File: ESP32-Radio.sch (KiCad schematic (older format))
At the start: 67 parts, among them J1 Jack-DC, J11 Conn_01x04_Female, J2 BNC, J6 Audio_Jack, Q1 2N3904-SMD, Q2 2SC5706, Q3 2SC5706, T1 T37_XFRM, U1 LM358, U10 si5351, U11 LD33V, U2 LM358, U6 MCP1703A-2502_SOT223, U8 FST3253

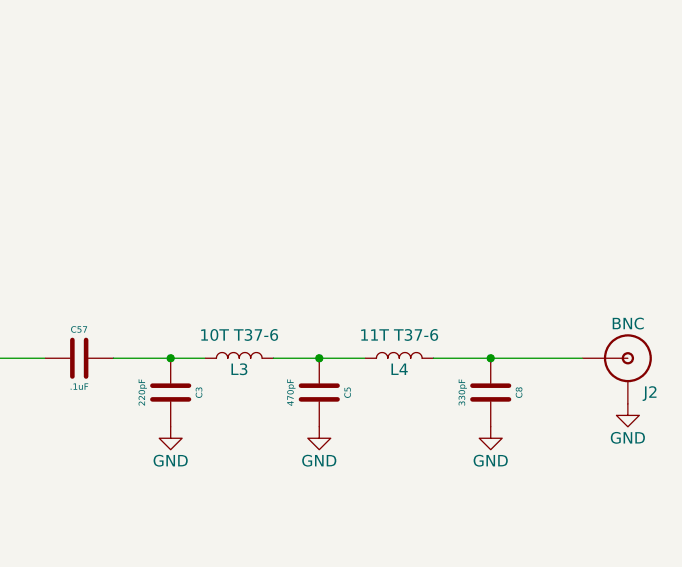
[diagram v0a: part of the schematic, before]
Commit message: added trap to lowpass
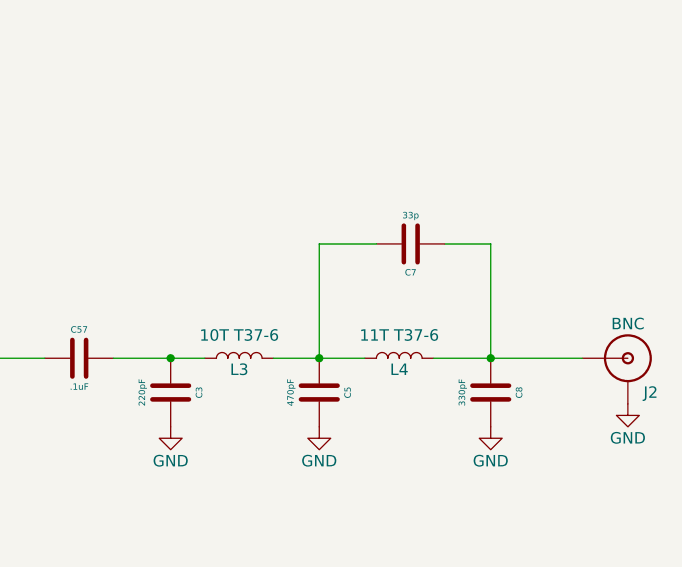
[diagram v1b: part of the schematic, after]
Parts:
- added C7: 33p, Xenir:Capacitor 1206, symbol Xenir:Capacitor
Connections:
- net at C8.1, J2.S (OUT), L4.2: now also C7.1
- net at C5.1, L3.2, L4.1: now also C7.2
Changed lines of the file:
@@
 	1    0    0    -1
 $EndComp
+$Comp
+L Xenir:Capacitor C7
+U 1 1 60F14082
+P 16550 7050
+F 0 "C7" H 16550 7175 28  0000 C CNN
+F 1 "33p" H 16550 6925 28  0000 C CNN
+F 2 "Xenir:Capacitor 1206" H 16550 6900 50  0001 C CNN
+F 3 "" H 16550 6900 50  0001 C CNN
+	1    16550 7050
+	-1   0    0    1
+$EndComp
+Wire Wire Line
+	16700 7050 16900 7050
+Wire Wire Line
+	16900 7050 16900 7550
+Wire Wire Line
+	16150 7050 16400 7050
+Wire Wire Line
+	16150 7050 16150 7550
 $EndSCHEMATC

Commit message: fixed rescue reference
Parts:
- removed R5: 1k, Xenir:Resistor 0805, symbol Xenir:Resistor
- removed T1: T37_XFRM, Xenir:T37 Transformer, symbol Xenir:T37_XFRM
- added C9: .1uF, Xenir:Capacitor 0805, symbol Xenir:Capacitor
- added R64, R65: 4.7k, Xenir:Resistor 0805, symbol Xenir:Resistor
- added R7, R8: 49.9, Xenir:Resistor 0805, symbol Xenir:Resistor
- added T1: T50_SPLITTER, Xenir:T50 Trifilar, symbol Xenir:T50_SPLITTER
- R4: symbol ESP32-Radio-rescue:0.3OHM-0805-1_8W-1%-phase_v3-eagle-import-IQ-Tayloe-Mixer-rescue -> Xenir:Resistor
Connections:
- net +2V5: now also T1.C2A, T1.C3B
- net +5V: now also R64.1
- net GND: now also R65.2, T1.C1B
- net at Q1.1 (B): now also C9.2, R64.2, R65.1
- net at U8.9 (2A): now also R7.2
- net at U8.7 (1A): now also R8.2
- new net: C9.1, T1.C1A
- new net: R8.1, T1.C2B
- new net: R7.1, T1.C3A
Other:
- moved on the sheet: J6
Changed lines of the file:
@@
 GND
 Wire Wire Line
-	9050 10700 9550 10700
-Wire Wire Line
 	10950 11600 11050 11600
 Wire Wire Line
@@
 Wire Wire Line
 	9150 12300 9150 11400
-$Comp
-L ESP32-Radio-rescue:GND-Tayloe_Detector_v5-eagle-import-IQ-Tayloe-Mixer-rescue #GND01
-U 1 1 12C122FD
-P 9550 11200
-F 0 "#GND01" H 9550 11200 50  0001 C CNN
-F 1 "GND" H 9550 11190 59  0000 C TNN
-F 2 "" H 9550 11200 50  0001 C CNN
-F 3 "" H 9550 11200 50  0001 C CNN
-	1    9550 11200
-	1    0    0    -1
-$EndComp
 $Comp
 L Xenir:Capacitor C30
@@
 $EndComp
 $Comp
-L ESP32-Radio-rescue:0.3OHM-0805-1_8W-1%-phase_v3-eagle-import-IQ-Tayloe-Mixer-rescue R4
+L Xenir:Resistor R4
 U 1 1 5EF82FCB
 P 3350 11900
@@
 	1    0    0    -1
 $EndComp
-Connection ~ 9550 11100
 Wire Wire Line
 	9550 10900 9550 11100
@@
 	0    1    1    0
 $EndComp
-Wire Wire Line
-	9300 9050 9300 10500
 Wire Wire Line
 	9300 10500 9550 10500
@@
 L Xenir:Audio_Jack J6
 U 1 1 5EBAA7D4
-P 1500 10350
-F 0 "J6" H 1100 10000 50  0000 C CNN
-F 1 "Audio_Jack" H 1500 10350 50  0000 C CNN
-F 2 "Xenir:Audio_Jack" H 1500 10350 50  0001 C CNN
-F 3 "" H 1500 10350 50  0001 C CNN
-	1    1500 10350
-	1    0    0    -1
-$EndComp
-Wire Wire Line
-	1700 10700 1700 10600
-Wire Wire Line
-	1700 10800 1700 10900
+P 1650 10400
+F 0 "J6" H 1250 10050 50  0000 C CNN
+F 1 "Audio_Jack" H 1650 10400 50  0000 C CNN
+F 2 "Xenir:Audio_Jack" H 1650 10400 50  0001 C CNN
+F 3 "" H 1650 10400 50  0001 C CNN
+	1    1650 10400
+	1    0    0    -1
+$EndComp
+Wire Wire Line
+	1850 10750 1850 10650
+Wire Wire Line
+	1850 10850 1850 10950
 $Comp
 L power:GND #PWR033
 U 1 1 5EC9FFD3
-P 2350 10550
-F 0 "#PWR033" H 2350 10300 50  0001 C CNN
-F 1 "GND" H 2350 10400 50  0000 C CNN
-F 2 "" H 2350 10550 50  0001 C CNN
-F 3 "" H 2350 10550 50  0001 C CNN
-	1    2350 10550
-	1    0    0    -1
-$EndComp
-Wire Wire Line
-	1700 10500 2350 10500
-Wire Wire Line
-	2350 10500 2350 10550
+P 2500 10600
+F 0 "#PWR033" H 2500 10350 50  0001 C CNN
+F 1 "GND" H 2500 10450 50  0000 C CNN
+F 2 "" H 2500 10600 50  0001 C CNN
+F 3 "" H 2500 10600 50  0001 C CNN
+	1    2500 10600
+	1    0    0    -1
+$EndComp
+Wire Wire Line
+	1850 10550 2500 10550
+Wire Wire Line
+	2500 10550 2500 10600
 $Comp
 L Xenir:Cap_Polarized C16
@@
 P 9300 6550
 F 0 "J11" H 9300 6750 50  0000 C CNN
-F 1 "Conn_01x04_Female" H 9300 6250 50  0000 C CNN
+F 1 "Conn_01x04_Female" V 9450 6550 50  0000 C CNN
 F 2 "Connector_PinHeader_2.54mm:PinHeader_1x04_P2.54mm_Vertical" H 9300 6550 50  0001 C CNN
 F 3 "~" H 9300 6550 50  0001 C CNN
@@
 $EndComp
 $Comp
-L Xenir:T37_XFRM T1
-U 1 1 60E9134B
-P 10150 8200
-F 0 "T1" H 10150 7350 50  0000 C CNN
-F 1 "T37_XFRM" H 10150 8200 50  0000 C CNN
-F 2 "Xenir:T37 Transformer" H 10150 8200 50  0001 C CNN
-F 3 "" H 10150 8200 50  0001 C CNN
-	1    10150 8200
-	1    0    0    -1
-$EndComp
-Wire Wire Line
-	9750 8950 9750 9150
-Wire Wire Line
-	9750 9150 10750 9150
-Wire Wire Line
-	10750 9150 10750 8350
-Wire Wire Line
-	10750 8350 10550 8350
-$Comp
-L Xenir:Resistor R5
-U 1 1 60EAA63C
-P 9300 8650
-F 0 "R5" H 9300 8725 28  0000 C CNN
-F 1 "1k" H 9300 8575 28  0000 C CNN
-F 2 "Xenir:Resistor 0805" H 9300 8550 50  0001 C CNN
-F 3 "" H 9300 8550 50  0001 C CNN
-	1    9300 8650
-	0    1    1    0
-$EndComp
-Wire Wire Line
-	9750 8350 9300 8350
-Wire Wire Line
-	9300 8350 9300 8450
-Wire Wire Line
-	10550 8950 10550 9050
-Wire Wire Line
-	10550 9050 9300 9050
-Wire Wire Line
-	9300 9050 9300 8850
-Connection ~ 9300 9050
-Wire Wire Line
-	9300 8350 9050 8350
-Wire Wire Line
-	9050 8350 9050 10700
-Connection ~ 9300 8350
-$Comp
 L Xenir:2N3904-SMD Q1
 U 1 1 60F3E262
@@
 	1    0    0    -1
 $EndComp
-Connection ~ 10750 8350
 $Comp
 L Xenir:Resistor R6
@@
 Wire Wire Line
 	6650 12000 7500 12000
-Text GLabel 1700 10800 2    50   Input ~ 0
+Text GLabel 1850 10850 2    50   Input ~ 0
 Q_Out
-Text GLabel 1700 10600 2    50   Input ~ 0
+Text GLabel 1850 10650 2    50   Input ~ 0
 I_Out
 Wire Wire Line
@@
 Wire Wire Line
 	16150 7050 16150 7550
+$Comp
+L Xenir:T50_SPLITTER T1
+U 1 1 60EFEA4B
+P 9850 9350
+F 0 "T1" H 9850 8100 50  0000 C CNN
+F 1 "T50_SPLITTER" H 9850 9250 50  0000 C CNN
+F 2 "Xenir:T50 Trifilar" H 9850 9350 50  0001 C CNN
+F 3 "" H 9850 9350 50  0001 C CNN
+	1    9850 9350
+	-1   0    0    1
+$EndComp
+Wire Wire Line
+	9500 8550 9500 8650
+$Comp
+L power:+2V5 #PWR0118
+U 1 1 60F29509
+P 9400 8650
+F 0 "#PWR0118" H 9400 8500 50  0001 C CNN
+F 1 "+2V5" H 9400 8790 50  0000 C CNN
+F 2 "" H 9400 8650 50  0001 C CNN
+F 3 "" H 9400 8650 50  0001 C CNN
+	1    9400 8650
+	1    0    0    -1
+$EndComp
+Wire Wire Line
+	9400 8650 9500 8650
+Connection ~ 9500 8650
+Wire Wire Line
+	9500 8650 9500 8750
+Wire Wire Line
+	9300 9150 9500 9150
+Wire Wire Line
+	9050 8150 9500 8150
+$Comp
+L Xenir:Capacitor C9
+U 1 1 60F4107E
+P 10350 8350
+F 0 "C9" H 10350 8475 28  0000 C CNN
+F 1 ".1uF" H 10350 8225 28  0000 C CNN
+F 2 "Xenir:Capacitor 0805" H 10350 8200 50  0001 C CNN
+F 3 "" H 10350 8200 50  0001 C CNN
+	1    10350 8350
+	1    0    0    -1
+$EndComp
+$Comp
+L power:GND #PWR0119
+U 1 1 60F42FA2
+P 10200 8950
+F 0 "#PWR0119" H 10200 8700 50  0001 C CNN
+F 1 "GND" H 10200 8800 50  0000 C CNN
+F 2 "" H 10200 8950 50  0001 C CNN
+F 3 "" H 10200 8950 50  0001 C CNN
+	1    10200 8950
+	1    0    0    -1
+$EndComp
+Wire Wire Line
+	10500 8350 10650 8350
+$Comp
+L Xenir:Resistor R64
+U 1 1 60F85DCA
+P 10650 8000
+F 0 "R64" H 10650 8075 28  0000 C CNN
+F 1 "4.7k" H 10650 7925 28  0000 C CNN
+F 2 "Xenir:Resistor 0805" H 10650 7900 50  0001 C CNN
+F 3 "" H 10650 7900 50  0001 C CNN
+	1    10650 8000
+	0    1    1    0
+$EndComp
+$Comp
+L Xenir:Resistor R65
+U 1 1 60F88DE3
+P 10650 8700
+F 0 "R65" H 10650 8775 28  0000 C CNN
+F 1 "4.7k" H 10650 8625 28  0000 C CNN
+F 2 "Xenir:Resistor 0805" H 10650 8600 50  0001 C CNN
+F 3 "" H 10650 8600 50  0001 C CNN
+	1    10650 8700
+	0    1    1    0
+$EndComp
+$Comp
+L power:GND #PWR04
+U 1 1 60F8A228
+P 10650 8900
+F 0 "#PWR04" H 10650 8650 50  0001 C CNN
+F 1 "GND" H 10650 8750 50  0000 C CNN
+F 2 "" H 10650 8900 50  0001 C CNN
+F 3 "" H 10650 8900 50  0001 C CNN
+	1    10650 8900
+	1    0    0    -1
+$EndComp
+$Comp
+L power:+5V #PWR03
+U 1 1 60F8A58E
+P 10650 7800
+F 0 "#PWR03" H 10650 7650 50  0001 C CNN
+F 1 "+5V" H 10650 7940 50  0000 C CNN
+F 2 "" H 10650 7800 50  0001 C CNN
+F 3 "" H 10650 7800 50  0001 C CNN
+	1    10650 7800
+	1    0    0    -1
+$EndComp
+Wire Wire Line
+	10650 8200 10650 8350
+Connection ~ 10650 8350
+Wire Wire Line
+	10650 8350 10750 8350
+Wire Wire Line
+	10650 8350 10650 8500
+$Comp
+L Xenir:Resistor R8
+U 1 1 60FC36BE
+P 9300 9850
+F 0 "R8" H 9300 9925 28  0000 C CNN
+F 1 "49.9" H 9300 9775 28  0000 C CNN
+F 2 "Xenir:Resistor 0805" H 9300 9750 50  0001 C CNN
+F 3 "" H 9300 9750 50  0001 C CNN
+	1    9300 9850
+	0    1    1    0
+$EndComp
+$Comp
+L Xenir:Resistor R7
+U 1 1 60FC45B4
+P 9050 9850
+F 0 "R7" H 9050 9925 28  0000 C CNN
+F 1 "49.9" H 9050 9775 28  0000 C CNN
+F 2 "Xenir:Resistor 0805" H 9050 9750 50  0001 C CNN
+F 3 "" H 9050 9750 50  0001 C CNN
+	1    9050 9850
+	0    1    1    0
+$EndComp
+Wire Wire Line
+	9300 9150 9300 9650
+Wire Wire Line
+	9050 10700 9550 10700
+Wire Wire Line
+	9300 10050 9300 10500
+Wire Wire Line
+	9050 10050 9050 10700
+Wire Wire Line
+	9050 8150 9050 9650
+$Comp
+L power:GND #PWR0120
+U 1 1 60F1D084
+P 9550 11100
+F 0 "#PWR0120" H 9550 10850 50  0001 C CNN
+F 1 "GND" H 9550 10950 50  0000 C CNN
+F 2 "" H 9550 11100 50  0001 C CNN
+F 3 "" H 9550 11100 50  0001 C CNN
+	1    9550 11100
+	1    0    0    -1
+$EndComp
+Connection ~ 9550 11100
 $EndSCHEMATC

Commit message: created
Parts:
- removed C21, C51, C52, C55: .1uF, Xenir:Capacitor 0805, symbol Xenir:Capacitor
- removed C4: 150pF, Xenir:Capacitor 1206, symbol Xenir:Capacitor
- removed C7: 33p, Xenir:Capacitor 1206, symbol Xenir:Capacitor
- removed D1: 1N914, Diode_SMD:D_SOD-323_HandSoldering, symbol Diode:1N914
- removed D2: D_Zener, Diode_THT:D_A-405_P10.16mm_Horizontal, symbol Device:D_Zener
- removed L2: Inductor, Xenir:T37_Inductor, symbol Xenir:Inductor
- removed Q3: 2SC5706, Package_TO_SOT_SMD:TO-252-2, symbol Xenir:2SC5706
- removed R54: 10k, Xenir:Resistor 0805, symbol Xenir:Resistor
- removed R55: 10, Xenir:Resistor 0805, symbol Xenir:Resistor
- removed R57: 1k, Xenir:Resistor 0805, symbol Xenir:Resistor
- removed R58: 100, Xenir:Resistor 0805, symbol Xenir:Resistor
- removed R59, R60: 1, Xenir:Resistor 1206, symbol Xenir:Resistor
- removed U11: LD33V, Package_TO_SOT_THT:TO-220-3_Vertical, symbol Xenir:LD33V
- added C103, C104, C110, C112, C15, C17, C19, C201, C202: .1uF, Xenir:Capacitor 0805, symbol Xenir:Capacitor
- added C18: 22uF, Xenir:Cap_4x5.4, symbol Xenir:Cap_Polarized
- added C207: 33p, Xenir:Capacitor 1206, symbol Xenir:Capacitor
- added D1: D_Zener, Diode_SMD:D_MiniMELF, symbol Device:D_Zener
- added J4: Audio_Jack, Xenir:Audio_Jack, symbol Xenir:Audio_Jack
- added Q3: BS170F, Package_TO_SOT_SMD:SOT-23, symbol Transistor_FET:BS170F
- added Q4: IRF510, Package_TO_SOT_THT:TO-220-3_Vertical, symbol Transistor_FET:IRF540N
- added Q5: IRFU9024, Package_TO_SOT_THT:TO-251-3_Vertical, symbol Xenir:IRFU9024
- added R101, R102: 18, Xenir:Resistor 0805, symbol Xenir:Resistor
- added R108: 100, Xenir:Resistor 0805, symbol Xenir:Resistor
- added R110: 62, Xenir:Resistor 0805, symbol Xenir:Resistor
- added R201: 33, Xenir:Resistor 0805, symbol Xenir:Resistor
- added R202: 10, Xenir:Resistor 0805, symbol Xenir:Resistor
- added R209: 2.7k, Xenir:Resistor 0805, symbol Xenir:Resistor
- added R93, R94, R97: 10k, Xenir:Resistor 0805, symbol Xenir:Resistor
- added R95: 1.5k, Xenir:Resistor 0805, symbol Xenir:Resistor
- added RV1, RV2: R_POT, Xenir:Trimpot Vertical, symbol Device:R_POT
- added T12: T37-43 25T:8T, Xenir:T37 Transformer, symbol Xenir:T37_XFRM
- added T13: T37-43 8T:4T, Xenir:T37 Transformer, symbol Xenir:T37_XFRM
- added U3: AMS1117, Package_TO_SOT_SMD:SOT-223-3_TabPin2, symbol Regulator_Linear:AMS1117
- C203: renamed from C3; value 220pF -> 150p
- C205: renamed from C5; value 470pF -> 330p
- C208: renamed from C8; value 330pF -> 150p
- L1: value Inductor -> T50-43 10T; footprint Xenir:T37_Inductor -> Xenir:T50_Inductor
- L3: value 10T T37-6 -> 14T T37-6
- L4: value 11T T37-6 -> 18T T37-6
- R106: renamed from R6; value 100 -> 62
- R52: value 1k -> 24k
- R53: value 1k -> 6.8k
- R64: value 4.7k -> 24k
- R65: value 4.7k -> 6.8k
- renumbered R7 to R147, R8 to R148
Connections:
- net +12V: now also C104.1, Q5.3 (S), R94.1, U3.3 (VI); no longer C53.1, C6.1, U6.1 (VI)
- net +2V5: now also C18.1, C19.1; no longer C16.1
- net +3V3: now also U3.2 (VO)
- net +5V: now also C110.1, RV2.3; no longer Q1.3 (C), R64.1
- net GND: now also C104.2, C110.2, C17.2, C18.2, C19.2, J4.SLEEVE, Q3.2 (S), Q4.3 (S), R101.2, R102.2, R108.2, R110.2, R201.2, R202.2, R93.1, RV1.3, RV2.1, T12.C2A, T13.C2A, U3.1 (ADJ)
- net at Q1.2 (E), R106.1: now also C112.1
- net at Q2.1 (B), R52.2, R53.1: now also C103.2
- net 12V-On: now reaches R52.1
- net 12V-On: now also C16.1, C53.1, R64.1, U6.1 (VI), C17.1, Q5.2 (D), T12.C1B, T13.C1B
- net at L1.2: now also C57.1, Q4.2 (D); no longer Q2.2 (C)
- net at Q2.3 (E): now also C15.1, R101.1
- net at C208.1, J2.S (OUT), L4.2: now also C207.1
- net at T1.C1A: now also RV1.1; no longer C9.1
- net at C205.1, L3.2, L4.1: now also C207.2
- new net: Q1.3 (C), T12.C1A
- new net: C9.1, RV1.2
- new net: C201.1, R108.1, T13.C2B
- new net: R209.1, RV2.2
- new net: C202.2, D1.1 (K), Q4.1 (G), R209.2
- new net: C112.2, R110.1
- new net: Q2.2 (C), T13.C1A
- new net: C201.2, C202.1, R201.1
- new net: C103.1, T12.C2B
- new net: D1.2 (A), R202.1
- new net: C15.2, R102.1
- new net: Q5.1 (G), R94.2, R97.1
- new net: Q3.3 (D), R97.2
- new net: C6.1, Q3.1 (G), R95.1
- new net: J4.RING, J4.RSH, J4.TIP, J4.TSH, R93.2, R95.2
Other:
- moved on the sheet: C1, C12, C13, C2, C203, C205, C208, C22, C23, C24, C25, C30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

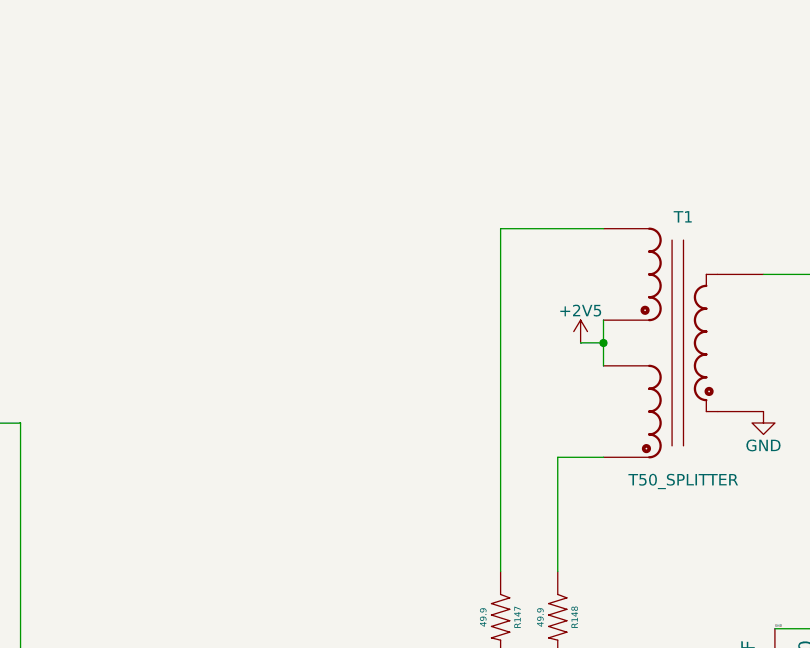
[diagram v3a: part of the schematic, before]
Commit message: added separate 2.5v to combiner
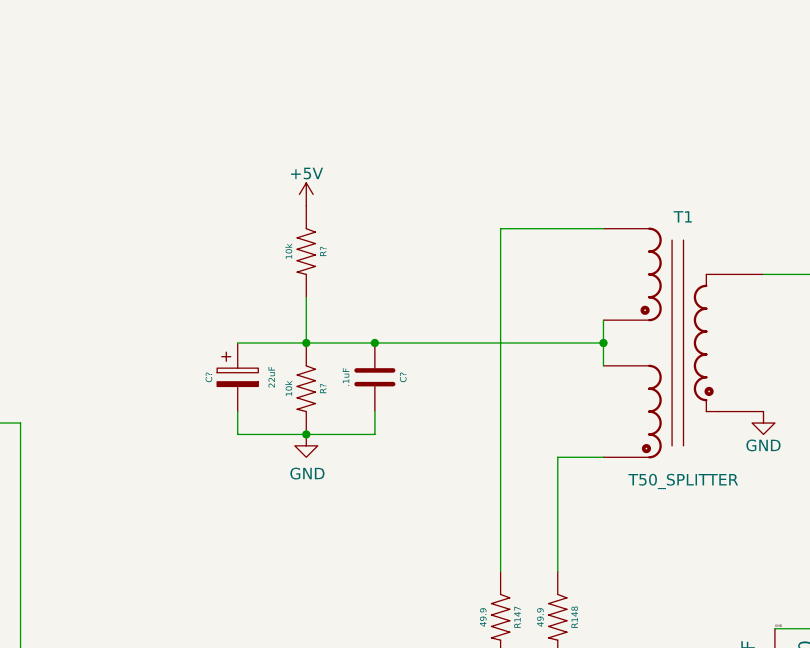
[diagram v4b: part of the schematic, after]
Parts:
- added C?: 22uF, Xenir:Cap_4x5.4, symbol Xenir:Cap_Polarized
- added C?: .1uF, Xenir:Capacitor 0805, symbol Xenir:Capacitor
- added R? (x2): 10k, Xenir:Resistor 0805, symbol Xenir:Resistor
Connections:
- net +2V5: no longer T1.C2A, T1.C3B
- net +5V: now also R?.1
- net GND: now also C?.2, C?.2, R?.2
- new net: C?.1, C?.1, R?.1, R?.2, T1.C2A, T1.C3B
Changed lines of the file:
@@
 Wire Wire Line
 	9850 9600 9850 9700
-$Comp
-L power:+2V5 #PWR0118
-U 1 1 60F29509
-P 9750 9700
-F 0 "#PWR0118" H 9750 9550 50  0001 C CNN
-F 1 "+2V5" H 9750 9840 50  0000 C CNN
-F 2 "" H 9750 9700 50  0001 C CNN
-F 3 "" H 9750 9700 50  0001 C CNN
-	1    9750 9700
-	1    0    0    -1
-$EndComp
-Wire Wire Line
-	9750 9700 9850 9700
 Connection ~ 9850 9700
 Wire Wire Line
@@
 Wire Wire Line
 	11650 9700 11300 9700
+$Comp
+L power:+5V #PWR?
+U 1 1 612306C4
+P 8550 9100
+F 0 "#PWR?" H 8550 8950 50  0001 C CNN
+F 1 "+5V" H 8550 9240 50  0000 C CNN
+F 2 "" H 8550 9100 50  0001 C CNN
+F 3 "" H 8550 9100 50  0001 C CNN
+	1    8550 9100
+	1    0    0    -1
+$EndComp
+$Comp
+L Xenir:Resistor R?
+U 1 1 612306CF
+P 8550 9300
+F 0 "R?" H 8550 9375 28  0000 C CNN
+F 1 "10k" H 8550 9225 28  0000 C CNN
+F 2 "Xenir:Resistor 0805" H 8550 9200 50  0001 C CNN
+F 3 "" H 8550 9200 50  0001 C CNN
+	1    8550 9300
+	0    1    1    0
+$EndComp
+$Comp
+L Xenir:Resistor R?
+U 1 1 612306DA
+P 8550 9900
+F 0 "R?" H 8550 9975 28  0000 C CNN
+F 1 "10k" H 8550 9825 28  0000 C CNN
+F 2 "Xenir:Resistor 0805" H 8550 9800 50  0001 C CNN
+F 3 "" H 8550 9800 50  0001 C CNN
+	1    8550 9900
+	0    1    1    0
+$EndComp
+$Comp
+L Xenir:Cap_Polarized C?
+U 1 1 612306E4
+P 8350 9850
+F 0 "C?" H 8350 9625 28  0000 C CNN
+F 1 "22uF" H 8350 9900 28  0000 C CNN
+F 2 "Xenir:Cap_4x5.4" H 8350 9900 50  0001 C CNN
+F 3 "" H 8350 9900 50  0001 C CNN
+	1    8350 9850
+	0    1    1    0
+$EndComp
+$Comp
+L Xenir:Capacitor C?
+U 1 1 612306EE
+P 8850 9850
+F 0 "C?" H 8850 9975 28  0000 C CNN
+F 1 ".1uF" H 8850 9725 28  0000 C CNN
+F 2 "Xenir:Capacitor 0805" H 8850 9700 50  0001 C CNN
+F 3 "" H 8850 9700 50  0001 C CNN
+	1    8850 9850
+	0    1    1    0
+$EndComp
+Wire Wire Line
+	8250 9700 8550 9700
+Wire Wire Line
+	8850 9700 8550 9700
+Connection ~ 8550 9700
+Wire Wire Line
+	8550 9500 8550 9700
+$Comp
+L power:GND #PWR?
+U 1 1 612306FC
+P 8550 10100
+F 0 "#PWR?" H 8550 9850 50  0001 C CNN
+F 1 "GND" H 8555 9927 50  0000 C CNN
+F 2 "" H 8550 10100 50  0001 C CNN
+F 3 "" H 8550 10100 50  0001 C CNN
+	1    8550 10100
+	1    0    0    -1
+$EndComp
+Wire Wire Line
+	8250 10000 8250 10100
+Wire Wire Line
+	8250 10100 8550 10100
+Connection ~ 8550 10100
+Wire Wire Line
+	8850 10000 8850 10100
+Wire Wire Line
+	8850 10100 8550 10100
+Wire Wire Line
+	8850 9700 9850 9700
+Connection ~ 8850 9700
 $EndSCHEMATC
